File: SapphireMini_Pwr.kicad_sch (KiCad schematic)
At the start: 23 parts, among them J501 JST, Q501 BC857BS, Q502 IRLML6402TRPBF, U501 TPS62150

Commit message: Minor changes to annotation
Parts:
- renumbered R509 to R502, R510 to R503, R511 to R504, R502 to R505, R503 to R506, R504 to R507, R505 to R508, R506 to R509, R507 to R510, R508 to R511
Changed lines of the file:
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@@
   (symbol (lib_id "Device:R_Small_US") (at 82.55 90.17 0) (unit 1)
     (in_bom yes) (on_board yes)
-    (property "Reference" "R502" (id 0) (at 84.2772 89.0016 0)
+    (property "Reference" "R505" (id 0) (at 84.2772 89.0016 0)
       (effects (font (size 1.27 1.27)) (justify left))
     )
@@
   (symbol (lib_id "power:GND") (at 82.55 109.22 0) (unit 1)
     (in_bom yes) (on_board yes)
-    (property "Reference" "#PWR0503" (id 0) (at 82.55 115.57 0)
+    (property "Reference" "#PWR0504" (id 0) (at 82.55 115.57 0)
       (effects (font (size 1.27 1.27)) hide)
     )
@@
   (symbol (lib_id "power:GND") (at 101.6 52.07 0) (unit 1)
     (in_bom yes) (on_board yes)
-    (property "Reference" "#PWR0504" (id 0) (at 101.6 58.42 0)
+    (property "Reference" "#PWR0505" (id 0) (at 101.6 58.42 0)
       (effects (font (size 1.27 1.27)) hide)
     )
@@
   (symbol (lib_id "power:GND") (at 110.49 52.07 0) (unit 1)
     (in_bom yes) (on_board yes)
-    (property "Reference" "#PWR0506" (id 0) (at 110.49 58.42 0)
+    (property "Reference" "#PWR0507" (id 0) (at 110.49 58.42 0)
       (effects (font (size 1.27 1.27)) hide)
     )
@@
   (symbol (lib_id "Device:R_Small_US") (at 82.55 104.14 0) (unit 1)
     (in_bom yes) (on_board yes)
-    (property "Reference" "R503" (id 0) (at 84.2772 102.9716 0)
+    (property "Reference" "R506" (id 0) (at 84.2772 102.9716 0)
       (effects (font (size 1.27 1.27)) (justify left))
     )
@@
   (symbol (lib_id "Device:R_Small_US") (at 148.59 90.17 270) (unit 1)
     (in_bom yes) (on_board yes)
-    (property "Reference" "R506" (id 0) (at 148.59 84.963 90))
+    (property "Reference" "R509" (id 0) (at 148.59 84.963 90))
     (property "Value" "100K" (id 1) (at 148.59 87.2744 90))
     (property "Footprint" "Resistor_SMD:R_0603_1608Metric" (id 2) (at 148.59 90.17 0)
@@
   (symbol (lib_id "Device:R_Small_US") (at 161.29 86.36 0) (unit 1)
     (in_bom yes) (on_board yes)
-    (property "Reference" "R507" (id 0) (at 163.0172 85.1916 0)
+    (property "Reference" "R510" (id 0) (at 163.0172 85.1916 0)
       (effects (font (size 1.27 1.27)) (justify left))
     )
@@
   (symbol (lib_id "Device:R_Small_US") (at 161.29 97.79 0) (unit 1)
     (in_bom yes) (on_board yes)
-    (property "Reference" "R508" (id 0) (at 163.0172 96.6216 0)
+    (property "Reference" "R511" (id 0) (at 163.0172 96.6216 0)
       (effects (font (size 1.27 1.27)) (justify left))
     )
@@
   (symbol (lib_id "power:GND") (at 134.62 104.14 0) (unit 1)
     (in_bom yes) (on_board yes)
-    (property "Reference" "#PWR0508" (id 0) (at 134.62 110.49 0)
+    (property "Reference" "#PWR0509" (id 0) (at 134.62 110.49 0)
       (effects (font (size 1.27 1.27)) hide)
     )
@@
   (symbol (lib_id "power:GND") (at 161.29 104.14 0) (unit 1)
     (in_bom yes) (on_board yes)
-    (property "Reference" "#PWR0509" (id 0) (at 161.29 110.49 0)
+    (property "Reference" "#PWR0510" (id 0) (at 161.29 110.49 0)
       (effects (font (size 1.27 1.27)) hide)
     )
@@
   (symbol (lib_id "power:GND") (at 168.91 104.14 0) (unit 1)
     (in_bom yes) (on_board yes)
-    (property "Reference" "#PWR0510" (id 0) (at 168.91 110.49 0)
+    (property "Reference" "#PWR0511" (id 0) (at 168.91 110.49 0)
       (effects (font (size 1.27 1.27)) hide)
     )
@@
   (symbol (lib_id "power:GND") (at 104.14 76.2 0) (unit 1)
     (in_bom yes) (on_board yes)
-    (property "Reference" "#PWR0505" (id 0) (at 104.14 82.55 0)
+    (property "Reference" "#PWR0506" (id 0) (at 104.14 82.55 0)
       (effects (font (size 1.27 1.27)) hide)
     )
@@
   (symbol (lib_id "power:GND") (at 110.49 104.14 0) (unit 1)
     (in_bom yes) (on_board yes)
-    (property "Reference" "#PWR0507" (id 0) (at 110.49 110.49 0)
+    (property "Reference" "#PWR0508" (id 0) (at 110.49 110.49 0)
       (effects (font (size 1.27 1.27)) hide)
     )
@@
   (symbol (lib_id "Device:R_Small_US") (at 118.11 74.93 0) (unit 1)
     (in_bom yes) (on_board yes)
-    (property "Reference" "R505" (id 0) (at 119.38 72.39 90)
+    (property "Reference" "R508" (id 0) (at 119.38 72.39 90)
       (effects (font (size 1.27 1.27)) (justify left))
     )
@@
   (symbol (lib_id "Device:R_Small_US") (at 96.52 64.77 90) (unit 1)
     (in_bom yes) (on_board yes)
-    (property "Reference" "R504" (id 0) (at 97.6884 66.4972 0)
+    (property "Reference" "R507" (id 0) (at 97.6884 66.4972 0)
       (effects (font (size 1.27 1.27)) (justify right))
     )
@@
   (symbol (lib_id "Device:R_Small_US") (at 67.31 130.81 0) (unit 1)
     (in_bom yes) (on_board yes)
-    (property "Reference" "R510" (id 0) (at 69.0372 129.6416 0)
+    (property "Reference" "R503" (id 0) (at 69.0372 129.6416 0)
       (effects (font (size 1.27 1.27)) (justify left))
     )
@@
   (symbol (lib_id "Device:R_Small_US") (at 67.31 123.19 0) (unit 1)
     (in_bom yes) (on_board yes)
-    (property "Reference" "R509" (id 0) (at 69.0372 122.0216 0)
+    (property "Reference" "R502" (id 0) (at 69.0372 122.0216 0)
       (effects (font (size 1.27 1.27)) (justify left))
     )
@@
   (symbol (lib_id "power:GND") (at 67.31 144.78 0) (unit 1)
     (in_bom yes) (on_board yes)
-    (property "Reference" "#PWR0102" (id 0) (at 67.31 151.13 0)
+    (property "Reference" "#PWR0503" (id 0) (at 67.31 151.13 0)
       (effects (font (size 1.27 1.27)) hide)
     )
@@
   (symbol (lib_id "Device:R_Small_US") (at 67.31 138.43 0) (unit 1)
     (in_bom yes) (on_board yes)
-    (property "Reference" "R511" (id 0) (at 69.0372 137.2616 0)
-      (effects (font (size 1.27 1.27)) (justify left))
-    )
+    (property "Reference" "R504" (id 0) (at 69.0372 137.2616 0)
+      (effects (font (size 1.27 1.27)) (justify left))
+    )

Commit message: Footprints complete. Starting layout
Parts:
- C501, C502: MPN GRM21BR61E106MA73L -> CL21A106KAYNNNE
- C503: MPN CL10B104KA8NNNC -> CL05A104KA5NNNC
- C505: MPN CGA5L1X5R1C226M160AC -> CL21A226MAYNNNE; Manufacturer TDK -> Samsung
- D501, J501, Q501: Status MiniReel -> (none)
- L501: footprint (none) -> SapphineMinimal:74439344022; MPN (none) -> 74439344022; Manufacturer (none) -> Würth Elektronik
- Q502: Status Active -> (none)
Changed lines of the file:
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@@
       (effects (font (size 1.27 1.27)) hide)
     )
-    (property "Status" "MiniReel" (id 14) (at 25.4 64.77 0)
+    (property "Status" "" (id 14) (at 25.4 64.77 0)
       (effects (font (size 1.27 1.27)) hide)
     )
@@
       (effects (font (size 1.27 1.27)) hide)
     )
-    (property "MPN" "CGA5L1X5R1C226M160AC" (id 5) (at 168.91 90.17 0)
+    (property "MPN" "CL21A226MAYNNNE" (id 5) (at 168.91 90.17 0)
       (effects (font (size 1.27 1.27)) hide)
     )
@@
       (effects (font (size 1.27 1.27)) hide)
     )
-    (property "Manufacturer" "TDK" (id 7) (at 168.91 90.17 0)
+    (property "Manufacturer" "Samsung" (id 7) (at 168.91 90.17 0)
       (effects (font (size 1.27 1.27)) hide)
     )
@@
       (effects (font (size 1.27 1.27)) hide)
     )
-    (property "Description" "22 µF ±20% 16V Ceramic Capacitor X5R 1206" (id 15) (at 168.91 90.17 0)
+    (property "Description" "22 µF ±20% 25V Ceramic Capacitor X5R 0805 (2012 Metric)" (id 15) (at 168.91 90.17 0)
       (effects (font (size 1.27 1.27)) hide)
     )
@@
       (effects (font (size 1.27 1.27)) hide)
     )
-    (property "Status" "MiniReel" (id 14) (at 59.69 80.01 0)
+    (property "Status" "" (id 14) (at 59.69 80.01 0)
       (effects (font (size 1.27 1.27)) hide)
     )
@@
       (effects (font (size 1.27 1.27)) hide)
     )
-    (property "Status" "MiniReel" (id 14) (at 80.01 80.01 0)
+    (property "Status" "" (id 14) (at 80.01 80.01 0)
       (effects (font (size 1.27 1.27)) hide)
     )
@@
       (effects (font (size 1.27 1.27)) hide)
     )
-    (property "Status" "MiniReel" (id 14) (at 88.9 50.8 0)
+    (property "Status" "" (id 14) (at 88.9 50.8 0)
       (effects (font (size 1.27 1.27)) hide)
     )
@@
       (effects (font (size 1.27 1.27)) hide)
     )
-    (property "MPN" "CL10B104KA8NNNC" (id 5) (at 110.49 48.26 0)
+    (property "MPN" "CL05A104KA5NNNC" (id 5) (at 110.49 48.26 0)
       (effects (font (size 1.27 1.27)) hide)
     )
@@
       (effects (font (size 1.27 1.27)) hide)
     )
-    (property "Description" "0.1 µF ±10% 25V Ceramic Capacitor X7R 0603 (1608 Metric)" (id 15) (at 110.49 48.26 0)
+    (property "Description" "0.1 µF ±10% 25V Ceramic Capacitor X5R 0402 (1005 Metric)" (id 15) (at 110.49 48.26 0)
       (effects (font (size 1.27 1.27)) hide)
     )
@@
       (effects (font (size 1.27 1.27)) hide)
     )
-    (property "MPN" "GRM21BR61E106MA73L" (id 6) (at 104.14 69.85 0)
+    (property "MPN" "CL21A106KAYNNNE" (id 6) (at 104.14 69.85 0)
       (effects (font (size 1.27 1.27)) hide)
     )
@@
       (effects (font (size 1.27 1.27)) hide)
     )
-    (property "Description" "10 µF ±20% 25V Ceramic Capacitor X5R 0805" (id 15) (at 104.14 69.85 0)
+    (property "Description" "10 µF ±10% 25V Ceramic Capacitor X5R 0805 (2012 Metric)" (id 15) (at 104.14 69.85 0)
       (effects (font (size 1.27 1.27)) hide)
     )
@@
       (effects (font (size 1.27 1.27)) hide)
     )
-    (property "MPN" "GRM21BR61E106MA73L" (id 6) (at 101.6 48.26 0)
+    (property "MPN" "CL21A106KAYNNNE" (id 6) (at 101.6 48.26 0)
       (effects (font (size 1.27 1.27)) hide)
     )
@@
       (effects (font (size 1.27 1.27)) hide)
     )
-    (property "Description" "10 µF ±20% 25V Ceramic Capacitor X5R 0805" (id 15) (at 101.6 48.26 0)
+    (property "Description" "10 µF ±10% 25V Ceramic Capacitor X5R 0805 (2012 Metric)" (id 15) (at 101.6 48.26 0)
       (effects (font (size 1.27 1.27)) hide)
     )
@@
       (effects (font (size 1.524 1.524)) (justify left) hide)
     )
-    (property "Status" "Active" (id 12) (at 38.1 59.69 0)
+    (property "Status" "" (id 12) (at 38.1 59.69 0)
       (effects (font (size 1.524 1.524)) (justify left) hide)
     )
@@
     (property "Reference" "L501" (id 0) (at 149.86 77.4532 90))
     (property "Value" "L_Iron" (id 1) (at 149.86 79.9901 90))
-    (property "Footprint" "" (id 2) (at 149.86 82.55 0)
+    (property "Footprint" "SapphineMinimal:74439344022" (id 2) (at 149.86 82.55 0)
       (effects (font (size 1.27 1.27)) hide)
     )
@@
       (effects (font (size 1.27 1.27)) hide)
     )
+    (property "Description" "FIXED IND 2.2UH 8A 10.5MOHM SMD" (id 4) (at 149.86 82.55 0)
+      (effects (font (size 1.27 1.27)) hide)
+    )
+    (property "MPN" "74439344022" (id 5) (at 149.86 82.55 0)
+      (effects (font (size 1.27 1.27)) hide)
+    )
+    (property "Manufacturer" "Würth Elektronik" (id 6) (at 149.86 82.55 0)
+      (effects (font (size 1.27 1.27)) hide)
+    )

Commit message: Working on update to power controllers
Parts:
- added C? (x4): 10uF, Capacitor_SMD:C_0805_2012Metric, symbol Device:C_Small
- added C?: 100nF, Capacitor_SMD:C_0603_1608Metric, symbol Device:C_Small
- added IC?: SLG59M1446V, SLG59M1446V, symbol SamacSys_Parts:SLG59M1446V
- added R? (x2): 20K0, symbol Device:R_US
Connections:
- net GND: now also C?.2, C?.2, C?.2, C?.2, C?.2, IC?.7 (GND)
- net P3V3: now also C?.1, C?.1, C?.1, IC?.1 (D2), IC?.4 (D1), IC?.6 (VDD)
- new net: IC?.3 (ON1), R?.2
- new net: IC?.2 (ON2), R?.2
- new net GNSS_OUTPUT_POWER: C?.1, IC?.5 (S1)
- new net GNSS_PWR: R?.1
- new net SD_OUTPUT_POWER: C?.1, IC?.8 (S2)
- new net SD_PWR: R?.1
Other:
- note added: "Battery Monitoring"
- note added: "DC-DC Power Supply"
- note added: "GNSS and SD power control"
- moved on the sheet: R502, R503, R504

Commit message: Checkpoint
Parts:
- added R512, R513: 100K, Resistor_SMD:R_0603_1608Metric, symbol Device:R_Small_US
- IC501: renamed from IC?; footprint SLG59M1446V -> SamacSys_Parts:SLG59M1446V
- R514, R515: renamed from R?; footprint (none) -> Resistor_SMD:R_0603_1608Metric
- gave numbers to parts that had none: 5
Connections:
- net GND: now also R513.2
- net GNSS_PWR: now also R513.1
- net P3V3: now also R512.1
- net SD_PWR: now also R512.2
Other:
- note added: "GNSS power defaults to off SD power defaults on on"

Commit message: Clean PCB but Added new clock to schematic
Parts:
- R514, R515: MPN (none) -> RMCF0603FT20K0; Manufacturer (none) -> Stackpole
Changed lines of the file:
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@@
+      (effects (font (size 1.27 1.27)) hide)
+    )
+    (property "MPN" "RMCF0603FT20K0" (id 4) (at 234.95 66.04 0)
+      (effects (font (size 1.27 1.27)) hide)
+    )
+    (property "Manufacturer" "Stackpole" (id 5) (at 234.95 66.04 0)
       (effects (font (size 1.27 1.27)) hide)
     )
@@
       (effects (font (size 1.27 1.27)) hide)
     )
+    (property "MPN" "RMCF0603FT20K0" (id 4) (at 234.95 63.5 0)
+      (effects (font (size 1.27 1.27)) hide)
+    )
+    (property "Manufacturer" "Stackpole" (id 5) (at 234.95 63.5 0)
+      (effects (font (size 1.27 1.27)) hide)
+    )

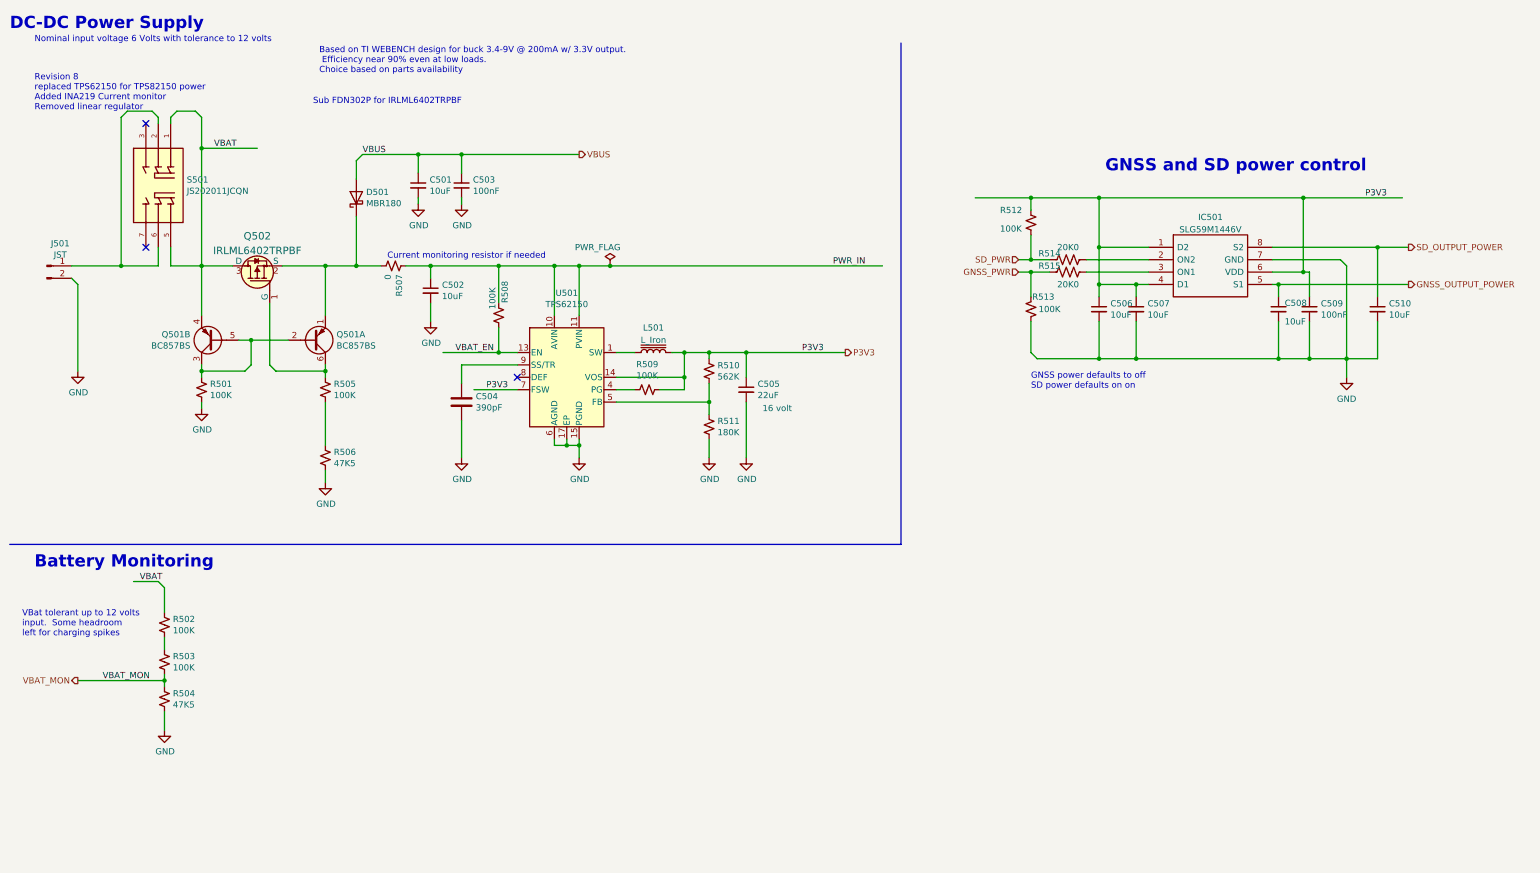
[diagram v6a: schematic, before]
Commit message: Updating for parts avail
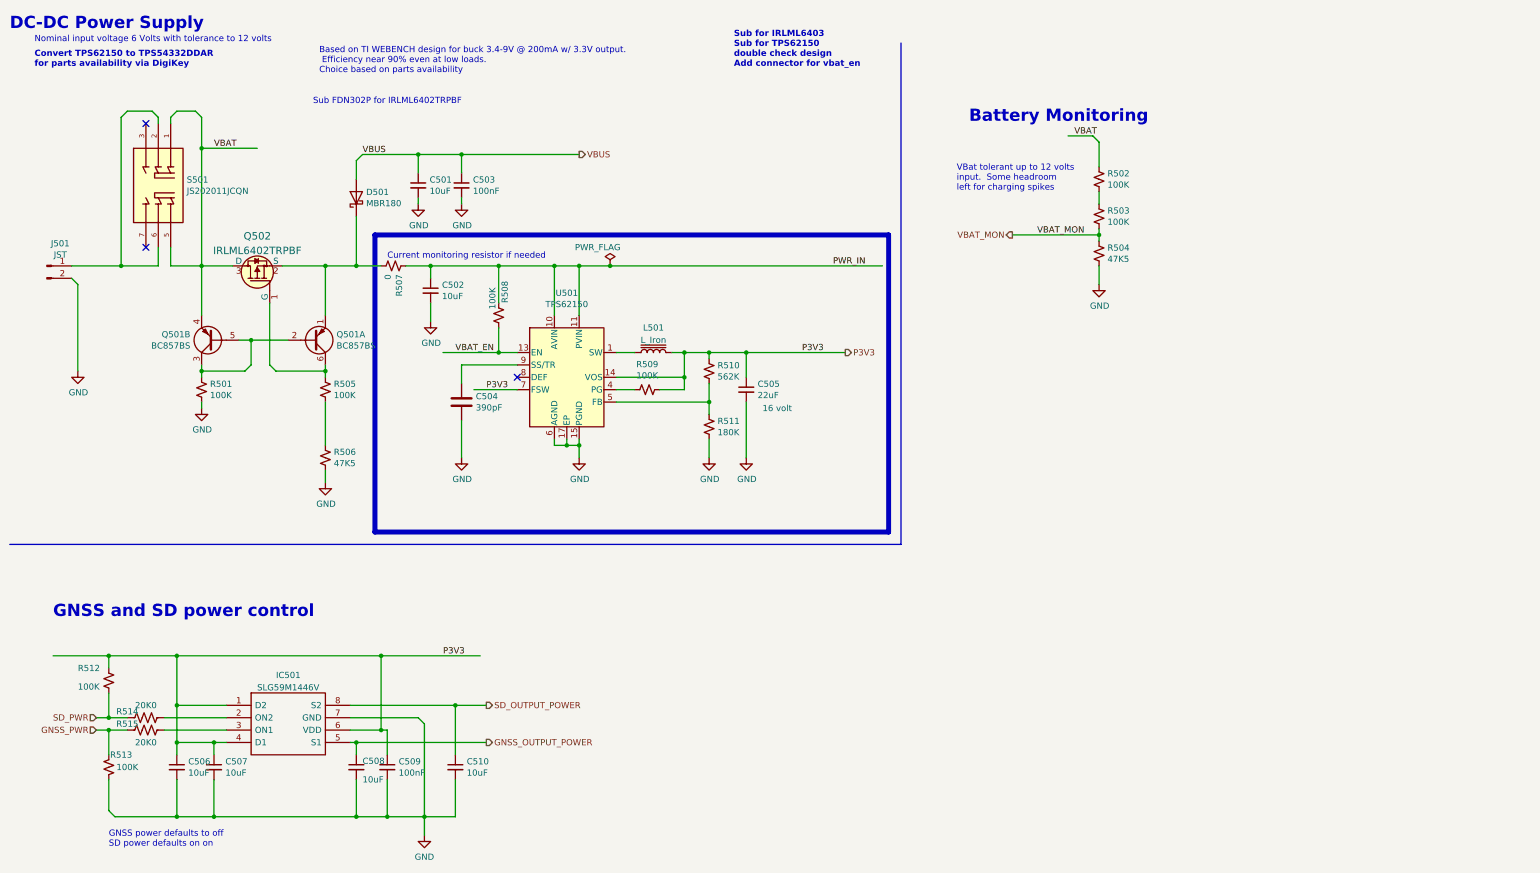
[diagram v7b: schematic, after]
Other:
- note added: "Convert TPS62150 to TPS54332DDAR for parts availability via DigiKey"
- note added: "Sub for IRLML6403 Sub for TPS62150 double check design Add connector for vbat_en"
- note removed: "Revision 8 replaced TPS62150 for TPS82150 power Added INA219 Current monitor Removed linear regulator"
- moved on the sheet: C506, C507, C508, C509, C510, IC501, R502, R503, R504, R512, R513, R514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
